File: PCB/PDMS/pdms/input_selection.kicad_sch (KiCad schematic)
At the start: 50 parts, among them U1 AQY221R4VY, U10 AQY221R4VY, U4 AQY221R4VY, U5 AQY221R4VY, U6 AQY221R4VY, U7 AQY221R4VY, U8 AQY221R4VY, U9 AQY221R4VY

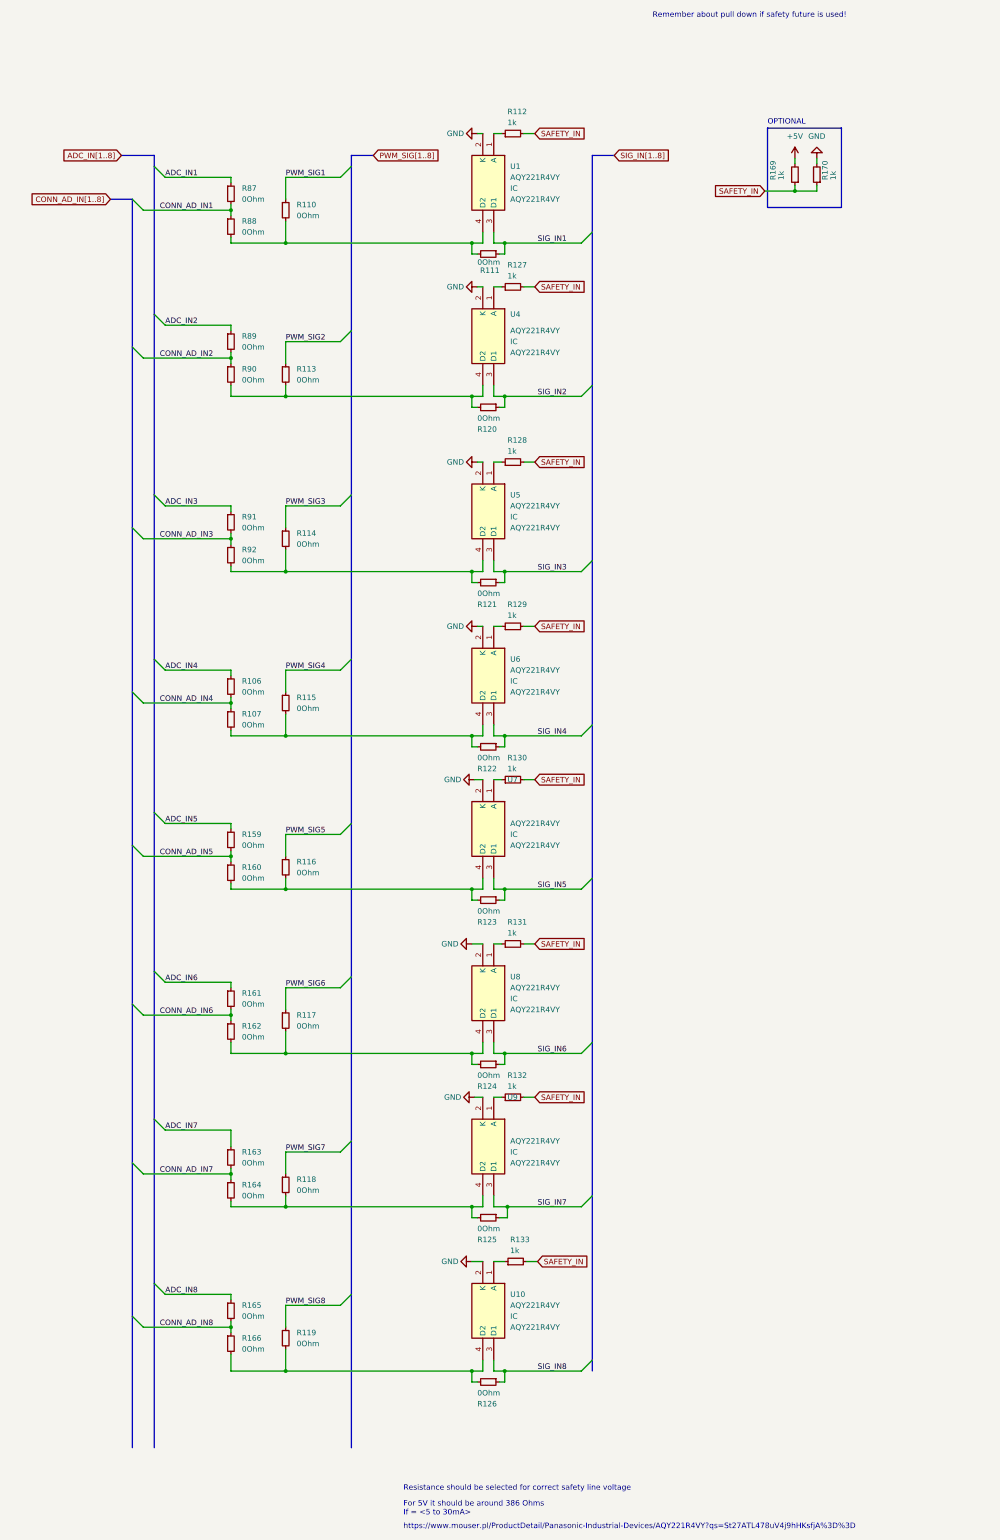
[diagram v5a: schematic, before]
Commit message: Centered HP section
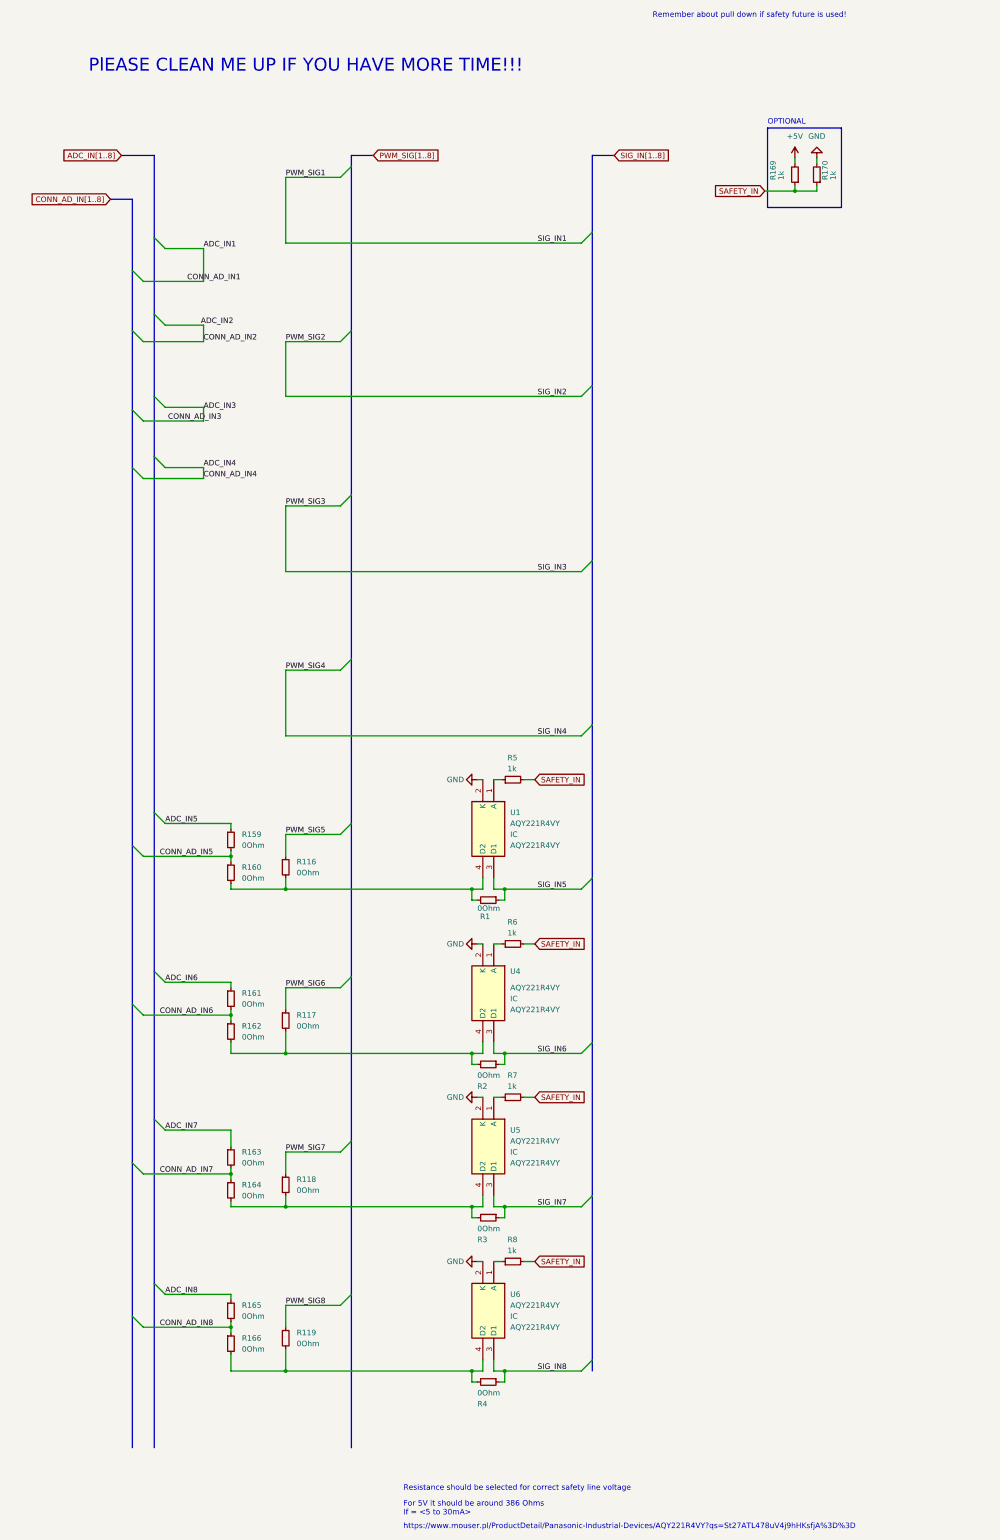
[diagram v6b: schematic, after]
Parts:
- removed R106, R107, R110, R111, R113, R114, R115, R120, R121, R122, R123, R124, R125, R126, R87, R88, R89, R90, R91, R92: 0Ohm, Resistor_SMD:R_0402_1005Metric, symbol Device:R_Small
- removed R112, R127, R128, R129, R130, R131, R132, R133: 1k, Resistor_SMD:R_0402_1005Metric, symbol Device:R_Small
- removed U10, U7, U8, U9: AQY221R4VY, PDMS_Additional:SOTFL127P485X190-4N, symbol pdms_additional:AQY221R4VY
- added R1, R2, R3, R4: 0Ohm, Resistor_SMD:R_0402_1005Metric, symbol Device:R_Small
- added R5, R6, R7, R8: 1k, Resistor_SMD:R_0402_1005Metric, symbol Device:R_Small
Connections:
- net SIG_IN1 is gone; now on net SIG_IN5: U1.3 (D1)
- net SIG_IN2 is gone; now on net SIG_IN6: U4.3 (D1)
- net SIG_IN3 is gone; now on net SIG_IN7: U5.3 (D1)
- net SIG_IN4 is gone; now on net SIG_IN8: U6.3 (D1)
- net SAFETY_IN: now also R5.2, R6.2, R7.2, R8.2
- net SIG_IN5: now also R1.1
- net SIG_IN6: now also R2.1
- net SIG_IN7: now also R3.1
- net SIG_IN8: now also R4.1
- net at U5.1 (A): now also R7.1
- net at U5.4 (D2): now also R118.2, R164.2, R3.2
- net at U6.1 (A): now also R8.1
- net at U6.4 (D2): now also R119.2, R166.2, R4.2
- net at R116.2, R160.2: now also U1.4 (D2), R1.2
- net at U4.4 (D2): now also R117.2, R162.2, R2.2
- net at U1.1 (A): now also R5.1
- net at U4.1 (A): now also R6.1
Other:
- note added: "PlEASE CLEAN ME UP IF YOU HAVE MORE TIME!!!"

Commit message: Finished layout - w/o stiching
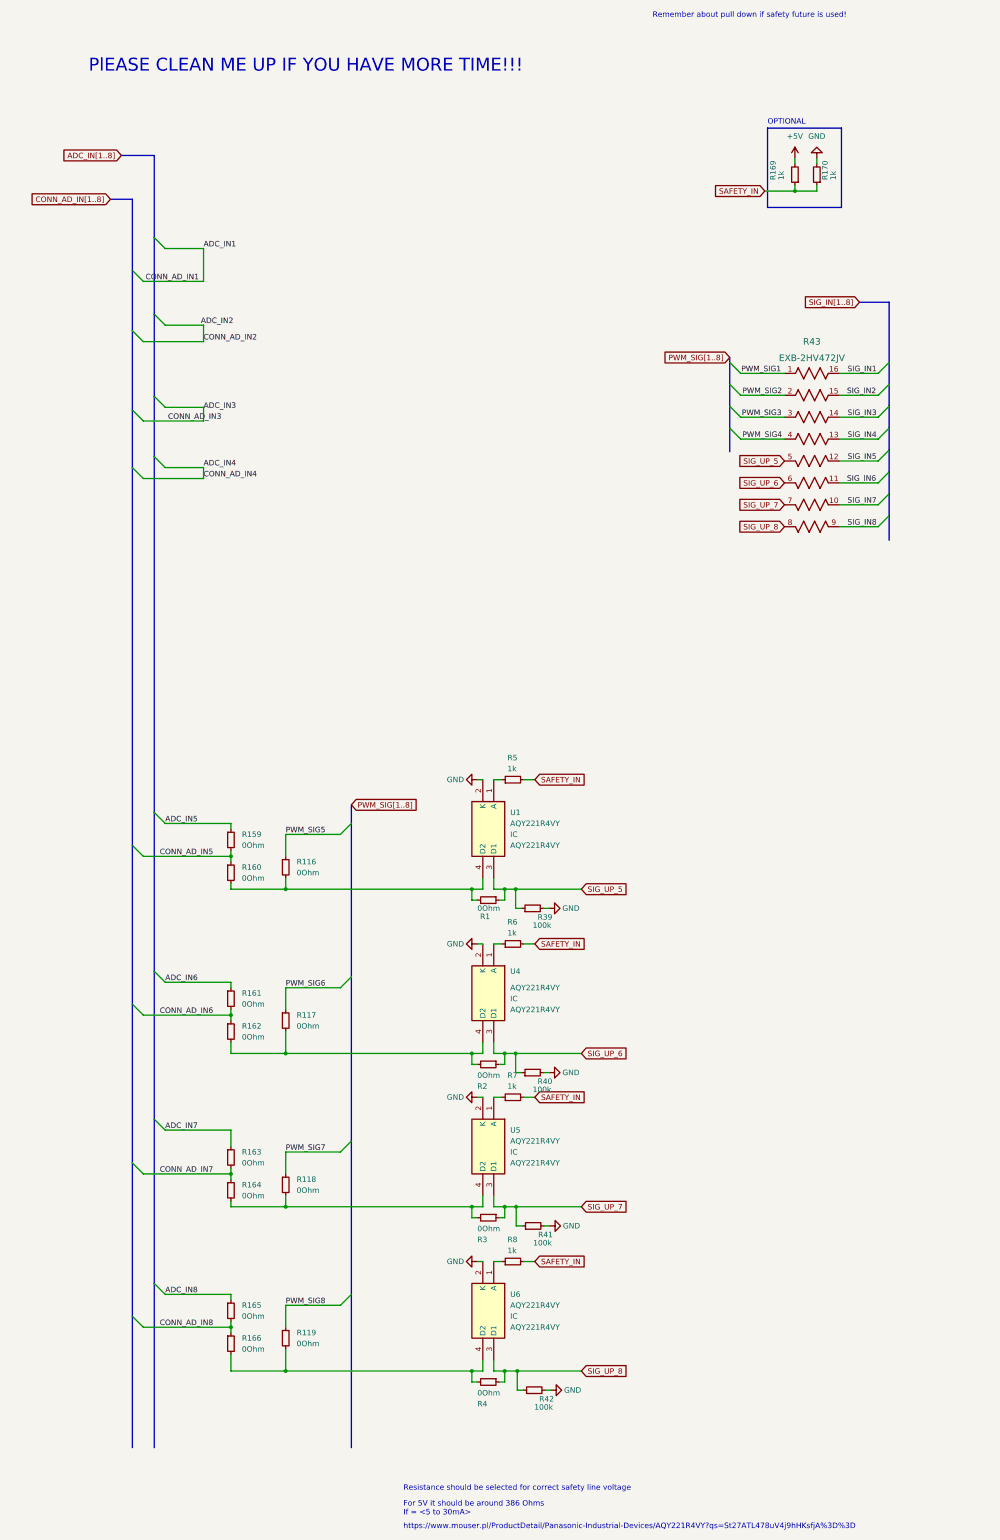
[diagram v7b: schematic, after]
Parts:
- added R39, R40, R41, R42: 100k, Resistor_SMD:R_0402_1005Metric, symbol Device:R_Small
- added R43: EXB-2HV472JV, PDMS_Additional:RES_EXB2HV, symbol pdms_additional:EXB-2HV472JV
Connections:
- net GND: now also R39.2, R40.2, R41.2, R42.2
- net PWM_SIG1: now also R43.1
- net PWM_SIG2: now also R43.2
- net PWM_SIG3: now also R43.3
- net PWM_SIG4: now also R43.4
- net SIG_IN5: now also R43.12; no longer R1.1, U1.3 (D1)
- net SIG_IN6: now also R43.11; no longer R2.1, U4.3 (D1)
- net SIG_IN7: now also R43.10; no longer R3.1, U5.3 (D1)
- net SIG_IN8: now also R43.9; no longer R4.1, U6.3 (D1)
- new net SIG_IN1: R43.16
- new net SIG_IN2: R43.15
- new net SIG_IN3: R43.14
- new net SIG_IN4: R43.13
- new net SIG_UP_5: R1.1, R39.1, R43.5, U1.3 (D1)
- new net SIG_UP_6: R2.1, R40.1, R43.6, U4.3 (D1)
- new net SIG_UP_7: R3.1, R41.1, R43.7, U5.3 (D1)
- new net SIG_UP_8: R4.1, R42.1, R43.8, U6.3 (D1)
